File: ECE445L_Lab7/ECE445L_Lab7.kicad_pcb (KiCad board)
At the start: 2 copper layers, 115 x 94 mm, 18 parts, among them Q1 IRLD024PBF, SW1 UP, SW2 DOWN, SW3 LEFT, SW4 RIGHT, SW5 MODE, U1 EK-TM4C123GXL, U2 Adafruit ST7735R, U3 ESP8266-01/ESP-01

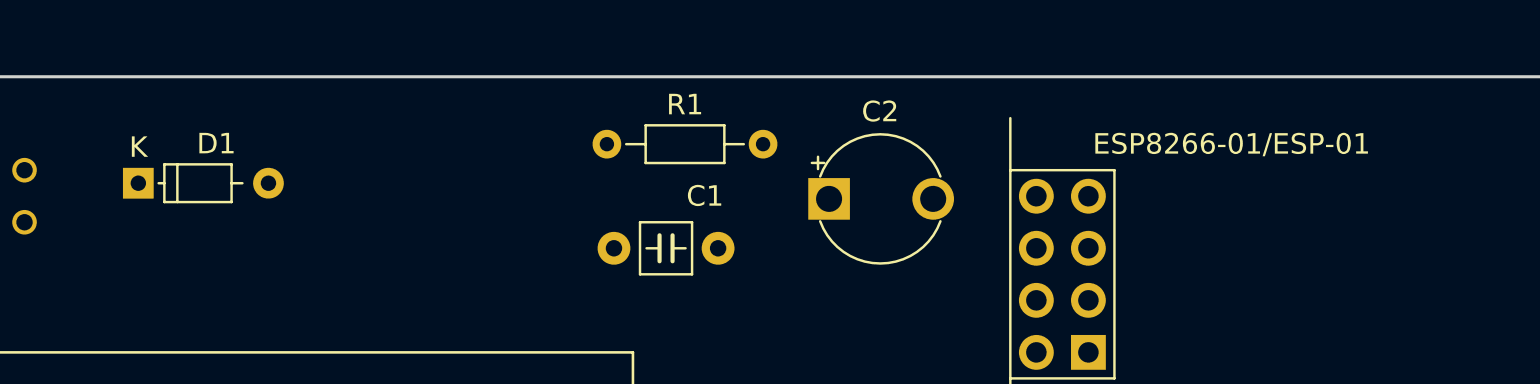
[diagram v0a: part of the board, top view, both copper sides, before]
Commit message: update all symbols and re-sync footprints in the KiCad projects
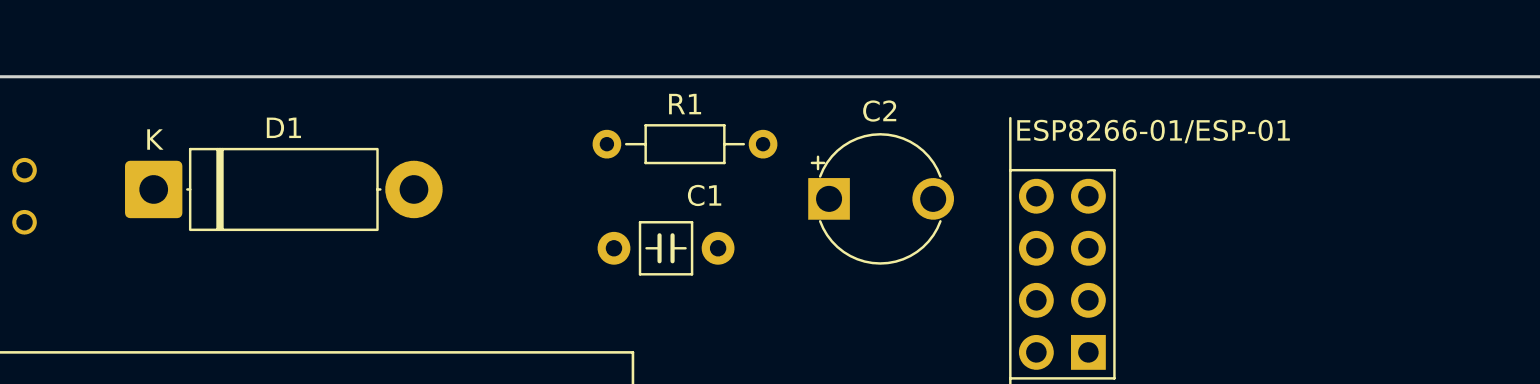
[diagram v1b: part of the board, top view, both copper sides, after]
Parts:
- D1: footprint ECE445L:D_P6.35mm_Horizontal -> Diode_THT:D_5W_P12.70mm_Horizontal
- U3: footprint ECE445L:PinHeader_2x04_P2.54mm_Vertical -> ECE445L:ESP8266_FemaleConnector
- moved D1 0.81 mm to (66.2, 36.5)
